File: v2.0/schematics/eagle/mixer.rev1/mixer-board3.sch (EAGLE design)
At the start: 5 parts, among them J1 RTN-1, J2 RTN-2, J3 SEND1, J4 SEND2

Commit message: Added stereo returns
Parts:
- added C1, C10, C11, C2, C4, C5, C7, C8: 100uF, _common:CE-USE5-8.5
- added C12, C3, C6, C9: (no value), _common:CC-US025-024X044
- added IC1, IC2: TL082P, _common:TL082P
- added JP1: (no value), pinhead:PINHD-2X8
- added R1, R13, R15, R7: 2.2K, _common:R
- added R10, R11, R12, R3, R4, R5, R6, R9: 10K, _common:R
- added R14, R16, R2, R8: 510, _common:R
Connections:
- new net +12V: JP1.5
- new net -12V: JP1.1
- new net 0V: J1.P$1, J1.P$2, J1.P$4, J2.P$1, J2.P$2, J2.P$4, JP1.3, R11.1, R12.1, R14.1, R16.1, R2.1, R5.1, R6.1, R8.1, RV1.1
- new net M2-LVL-2: JP1.9, RV1.2
- new net M2-LVL-3: JP1.7, RV1.3
- new net N$1: C1.+, J1.P$3, J1.P$6
- new net N$10: C2.-, R4.1
- new net N$11: IC2B.+IN, R10.2, R12.2
- new net N$12: IC2A.+IN, R11.2, R9.2
- new net N$13: C9.2, IC2A.-IN, R13.1, R14.2
- new net N$14: C10.+, C9.1, IC2A.OUT, R13.2
- new net N$15: C7.-, R9.1
- new net N$16: C8.-, R10.1
- new net N$17: C12.2, IC2B.-IN, R15.1, R16.2
- new net N$18: C11.+, C12.1, IC2B.OUT, R15.2
- new net N$19: C7.+, J2.P$3, J2.P$6
- new net N$2: C2.+, J1.P$5
- new net N$20: C8.+, J2.P$5
- new net N$3: C6.2, IC1B.-IN, R1.1, R2.2
- new net N$4: C5.+, C6.1, IC1B.OUT, R1.2
- new net N$5: IC1B.+IN, R4.2, R6.2
- new net N$6: IC1A.+IN, R3.2, R5.2
- new net N$7: C3.2, IC1A.-IN, R7.1, R8.2
- new net N$8: C1.-, R3.1
- new net N$9: C3.1, C4.+, IC1A.OUT, R7.2
- new net RTN1-L: C5.-, JP1.2
- new net RTN1-R: C4.-, JP1.4
- new net RTN2-L: C11.-, JP1.6
- new net RTN2-R: C10.-, JP1.8
- new net SEND1: JP1.11
- new net SEND2: JP1.13
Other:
- note added: "For mono in, push to first click"
- note added: "N/C"
- moved on the sheet: J1, J2, J3, J4, RV1

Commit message: Completed initial mixer schematic draft
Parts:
- added C13, C14, C15, C16: 22pF, _common:CC-US025-024X044
- added C17, C18: 100uF, _common:CE-USE2-5
- added C19, C20, C21, C22, C25, C26, C27, C28, C29, C30: 0.1uF, _common.v1:CC-US025-024X044
- added C23, C24: 10uF, _common.v1:CE-USE2-5
- added IC3, IC4: TL082P, _common:TL082P
- added R17, R18, R19, R20: 100K, _common:R
- added R21, R22: 22K, _common:R
- added R23, R24, R25, R26, R27, R28: 10K, _common:R
- C12, C3, C9: value (none) -> 100uF; device _common:CC-US025-024X044 -> _common:CE-USE5-8.5
- C5, C7, C8: value 100uF -> 22pF; device _common:CE-USE5-8.5 -> _common:CC-US025-024X044
- C6: value (none) -> 22pF
- R1, R7: value 2.2K -> 10K
- R10, R11, R12, R9: value 10K -> 10k
- R13, R15: value 2.2K -> 30k
- R14, R16: value 510 -> 30k
- R2, R8: value 510 -> 10K
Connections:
- new net N$21: C13.2, IC3A.-IN, R17.2, R19.2, R21.1
- new net N$22: C13.1, IC3A.OUT, R21.2, R23.1
- new net N$23: C15.2, IC3B.-IN, R23.2, R25.1
- new net N$24: C15.1, C17.-, IC3B.OUT, R25.2
- new net N$25: C14.2, IC4A.-IN, R18.2, R20.2, R22.1
- new net N$26: C14.1, IC4A.OUT, R22.2, R24.1
- new net N$27: C16.2, IC4B.-IN, R24.2, R26.1
- new net N$28: C16.1, C18.-, IC4B.OUT, R26.2
- new net OUT-LVL-1: C18.+, J4.P$3, R28.2
- new net OUT-LVL-6: C17.+, J3.P$3, R27.2
- net +12V: now also C19.1, C21.1, C23.+, C25.1, C27.1, C29.1
- net -12V: now also C20.2, C22.2, C24.-, C26.2, C28.2, C30.2
- net 0V: now also C19.2, C20.1, C21.2, C22.1, C23.-, C24.+, C25.2, C26.1, C27.2, C28.1, C29.2, C30.1, IC3A.+IN, IC3B.+IN, IC4A.+IN, IC4B.+IN, J3.P$1, J3.P$2, J4.P$1, J4.P$2, R10.1, R19.1, R20.1, R27.1, R28.1, R7.1, R9.1; no longer R14.1, R16.1, R2.1
- net N$10: now also R2.1; no longer R4.1
- net N$11: now also R4.2, R8.2; no longer R10.2, R12.2
- net N$12: now also R3.2, R7.2; no longer R11.2, R9.2
- net N$13: now also C7.2, R11.2, R15.1; no longer C9.2, R13.1, R14.2
- net N$14: now also C11.+, C7.1, R15.2; no longer C10.+, C9.1, R13.2
- net N$15: now also C3.-, R3.1; no longer C7.-, R9.1
- net N$16: now also C4.-, R4.1; no longer C8.-, R10.1
- net N$17: now also C8.2, R12.2, R16.1; no longer C12.2, R15.1, R16.2
- net N$18: now also C12.+, C8.1, R16.2; no longer C11.+, C12.1, R15.2
- net N$19: now also C3.+; no longer C7.+
- net N$20: now also C4.+; no longer C8.+
- net N$3: now also R10.2, R14.1; no longer R1.1, R2.2
- net N$4: now also C10.+, R14.2; no longer C5.+, R1.2
- net N$5: now also R2.2; no longer R4.2
- net N$6: now also R1.2; no longer R3.2
- net N$7: now also C5.2, R13.1, R9.2; no longer C3.2, R7.1, R8.2
- net N$8: now also R1.1; no longer R3.1
- net N$9: now also C5.1, C9.+, R13.2; no longer C3.1, C4.+, R7.2
- net RTN1-L: now also C10.-; no longer C5.-
- net RTN1-R: now also C9.-; no longer C4.-
- net RTN2-L: now also C12.-; no longer C11.-
- net RTN2-R: now also C11.-; no longer C10.-
- net SEND1: now also R17.1
- net SEND2: now also R18.1
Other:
- moved on the sheet: C1, C10, C11, C12, C2, C3, C4, C5, C6, C7, C8, C9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

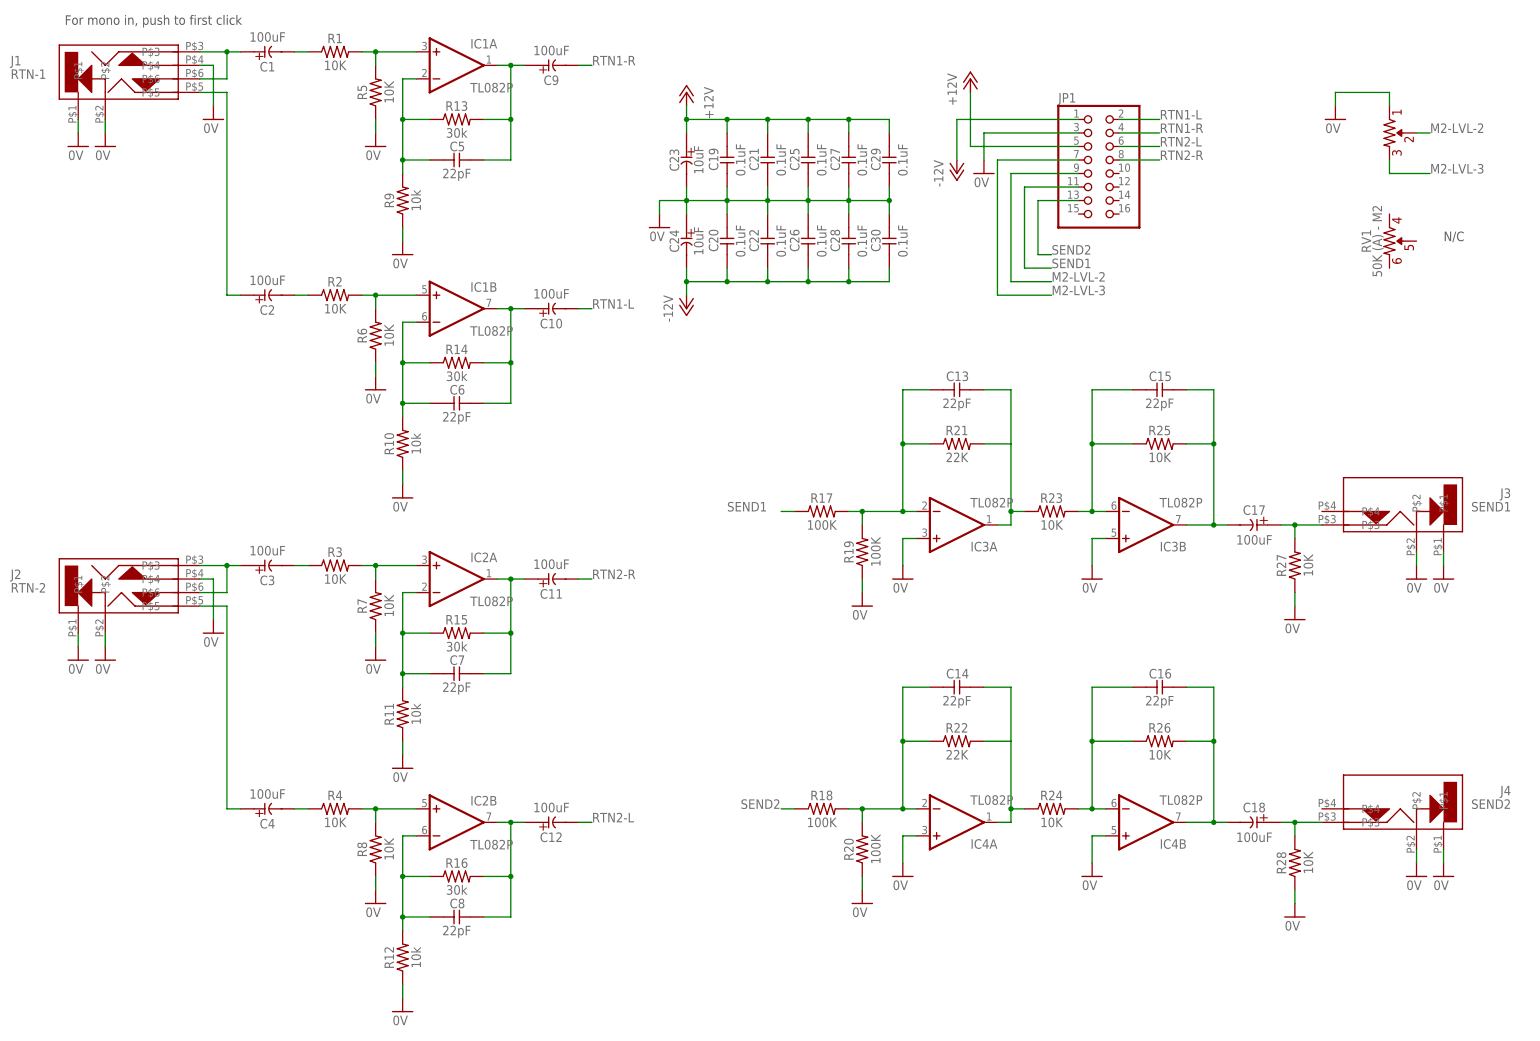
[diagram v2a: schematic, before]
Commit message: Updated VAR-ST; Added FX Crossfades; Ran error checks
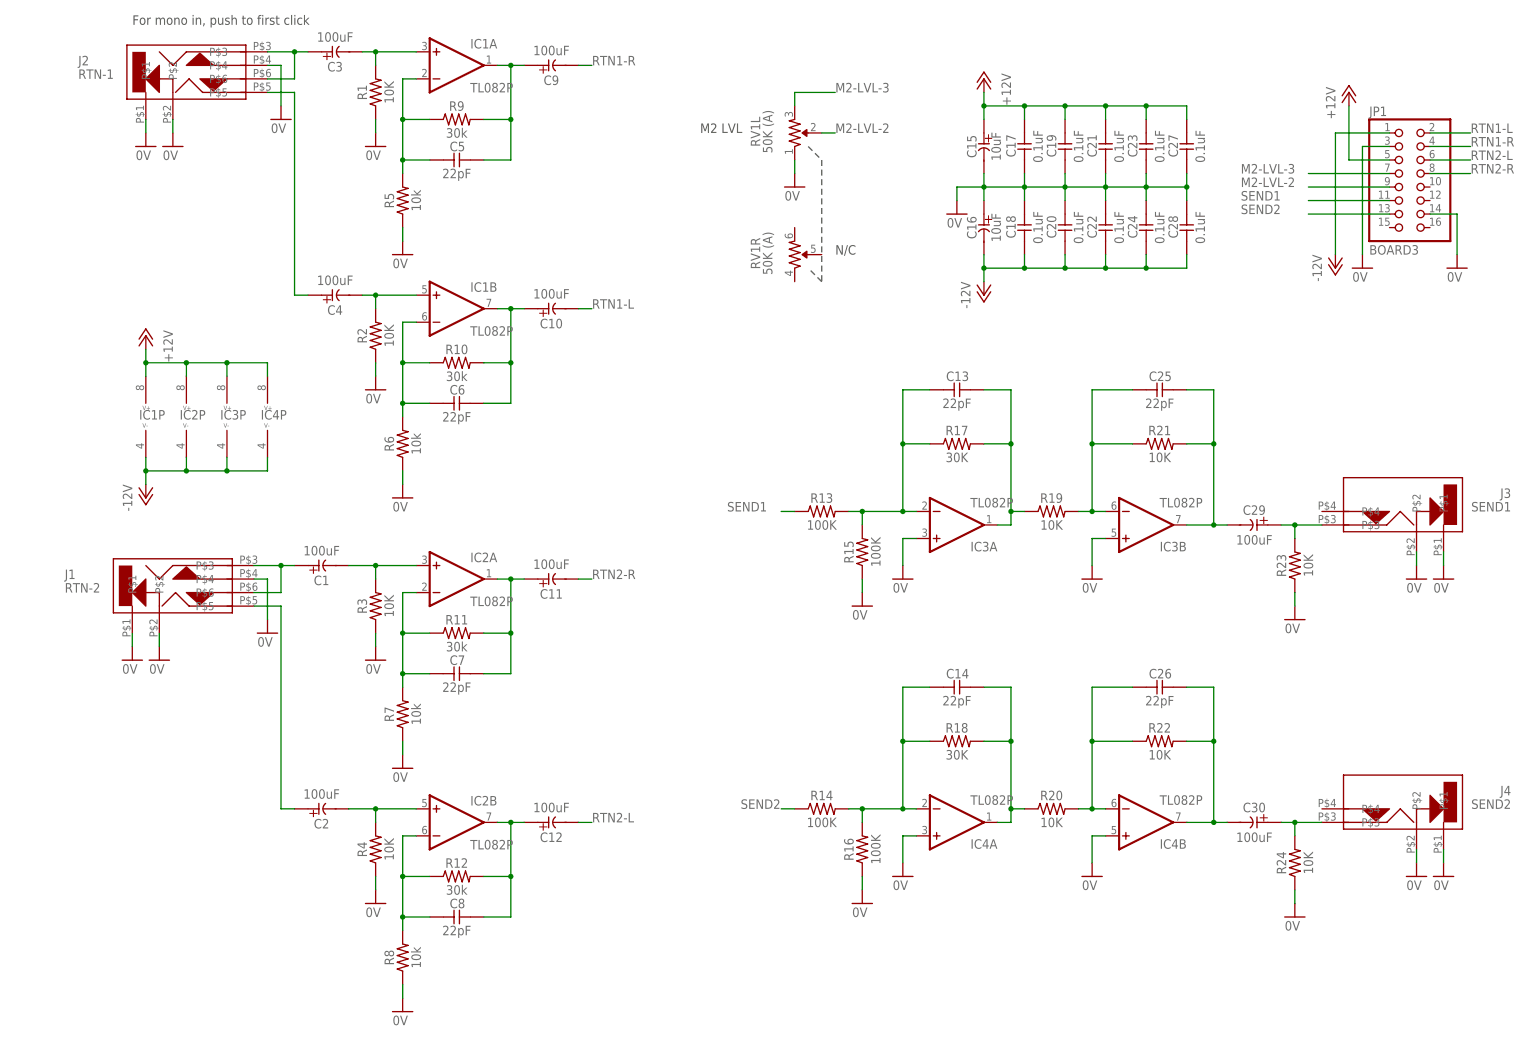
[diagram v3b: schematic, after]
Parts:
- removed R25, R26, R27, R28: 10K, _common:R
- C15, C16: value 22pF -> 10uF; device _common:CC-US025-024X044 -> _common.v1:CE-USE2-5
- C17, C18: value 100uF -> 0.1uF; device _common:CE-USE2-5 -> _common.v1:CC-US025-024X044
- C23, C24: value 10uF -> 0.1uF; device _common.v1:CE-USE2-5 -> _common.v1:CC-US025-024X044
- C25, C26: value 0.1uF -> 22pF; device _common.v1:CC-US025-024X044 -> _common:CC-US025-024X044
- C29, C30: value 0.1uF -> 100uF; device _common.v1:CC-US025-024X044 -> _common:CE-USE2-5
- J1: value RTN-1 -> RTN-2
- J2: value RTN-2 -> RTN-1
- JP1: value (none) -> BOARD3
- R10, R11, R12, R9: value 10k -> 30k
- R13, R14, R15, R16: value 30k -> 100K
- R17, R18: value 100K -> 30K
- R19, R20: value 100K -> 10K
- R21, R22: value 22K -> 10K
- R5, R6, R7, R8: value 10K -> 10k
- RV1: value 50K (A) - M2 -> 50K (A)
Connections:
- removed net N$11: IC2B.+IN, R4.2, R8.2
- removed net N$12: IC2A.+IN, R3.2, R7.2
- removed net N$5: IC1B.+IN, R2.2, R6.2
- removed net N$8: C1.-, R1.1
- net +12V: now also C15.+, C17.1, C23.1, IC1P.V+, IC2P.V+, IC3P.V+, IC4P.V+; no longer C23.+, C25.1, C29.1
- net -12V: now also C16.-, C18.2, C24.2, IC1P.V-, IC2P.V-, IC3P.V-, IC4P.V-; no longer C24.-, C26.2, C30.2
- net 0V: now also C15.-, C16.+, C17.2, C18.1, C23.2, C24.1, JP1.14, R1.1, R15.1, R16.1, R2.1, R23.1, R24.1, R3.1, R4.1, RV1L.1; no longer C23.-, C24.+, C25.2, C26.1, C29.2, C30.1, R10.1, R11.1, R12.1, R19.1, R20.1, R27.1, R28.1, R9.1, RV1.1
- net M2-LVL-2: now also RV1L.2; no longer RV1.2
- net M2-LVL-3: now also RV1L.3; no longer RV1.3
- net N$10: now also C4.-, IC1B.+IN, R2.2; no longer C2.-, R2.1
- net N$13: now also R11.1, R7.2; no longer R11.2, R15.1
- net N$14: now also R11.2; no longer R15.2
- net N$15: now also C1.-, IC2A.+IN, R3.2; no longer C3.-, R3.1
- net N$16: now also C2.-, IC2B.+IN, R4.2; no longer C4.-, R4.1
- net N$17: now also R12.1, R8.2; no longer R12.2, R16.1
- net N$18: now also R12.2; no longer R16.2
- net N$21: now also R13.2, R15.2, R17.1; no longer R17.2, R19.2, R21.1
- net N$22: now also R17.2, R19.1; no longer R21.2, R23.1
- net N$23: now also C25.2, R19.2, R21.1; no longer C15.2, R23.2, R25.1
- net N$24: now also C25.1, C29.-, R21.2; no longer C15.1, C17.-, R25.2
- net N$25: now also R14.2, R16.2, R18.1; no longer R18.2, R20.2, R22.1
- net N$26: now also R18.2, R20.1; no longer R22.2, R24.1
- net N$27: now also C26.2, R20.2, R22.1; no longer C16.2, R24.2, R26.1
- net N$28: now also C26.1, C30.-, R22.2; no longer C16.1, C18.-, R26.2
- net N$3: now also R10.1, R6.2; no longer R10.2, R14.1
- net N$4: now also R10.2; no longer R14.2
- net N$6: now also C3.-; no longer R5.2
- net N$7: now also R5.2, R9.1; no longer R13.1, R9.2
- net N$9: now also R9.2; no longer R13.2
- net OUT-LVL-1: now also C30.+, R24.2; no longer C18.+, R28.2
- net OUT-LVL-6: now also C29.+, R23.2; no longer C17.+, R27.2
- net SEND1: now also R13.1; no longer R17.1
- net SEND2: now also R14.1; no longer R18.1
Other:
- note added: "M2 LVL"
- moved on the sheet: C1, C15, C16, C17, C18, C19, C2, C20, C21, C22, C23, C24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

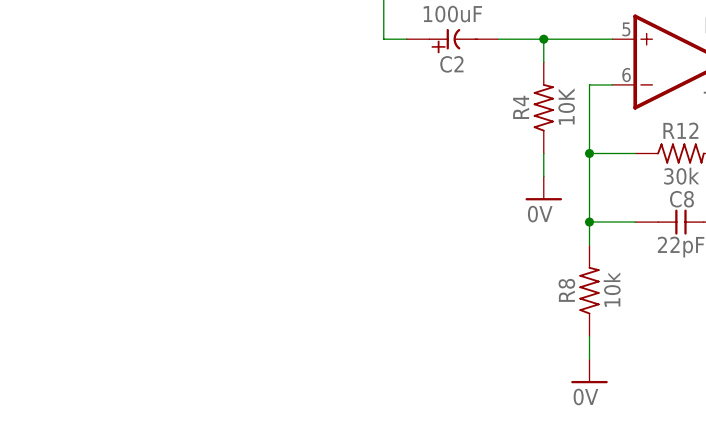
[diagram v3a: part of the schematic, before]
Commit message: Added schem titles
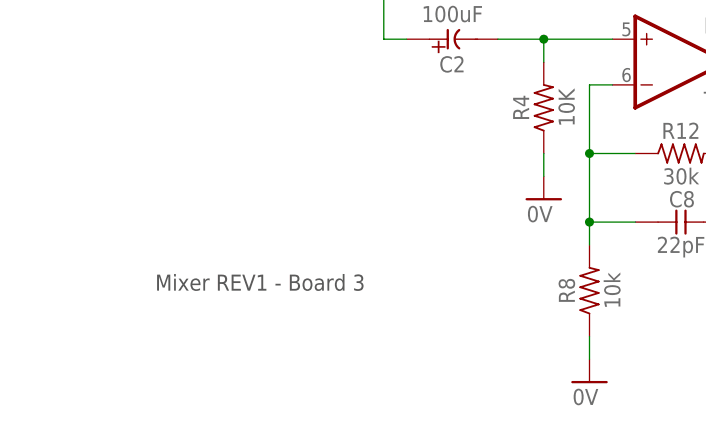
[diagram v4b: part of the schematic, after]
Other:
- note added: "Mixer REV1 - Board 3"
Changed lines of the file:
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@@
 <wire x1="177.8" y1="129.54" x2="177.8" y2="106.68" width="0.1524" layer="97" style="shortdash"/>
 <wire x1="177.8" y1="106.68" x2="175.26" y2="109.22" width="0.1524" layer="97" style="shortdash"/>
+<text x="50.8" y="-20.32" size="1.778" layer="97">Mixer REV1 - Board 3</text>
 </plain>
 <instances>

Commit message: Updated cap packages
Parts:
- C29, C30: device _common:CE-USE2-5 -> _common:CE-USE5-8.5
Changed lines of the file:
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@@
 <part name="GND19" library="supply1" library_urn="urn:adsk.eagle:library:371" deviceset="0V" device=""/>
 <part name="GND20" library="supply1" library_urn="urn:adsk.eagle:library:371" deviceset="0V" device=""/>
-<part name="C29" library="_common" deviceset="CE-US" device="E2-5" value="100uF"/>
+<part name="C29" library="_common" deviceset="CE-US" device="E5-8.5" value="100uF"/>
 <part name="R23" library="_common" deviceset="R" device="" value="10K"/>
 <part name="GND21" library="supply1" library_urn="urn:adsk.eagle:library:371" deviceset="0V" device=""/>
@@
 <part name="GND23" library="supply1" library_urn="urn:adsk.eagle:library:371" deviceset="0V" device=""/>
 <part name="GND24" library="supply1" library_urn="urn:adsk.eagle:library:371" deviceset="0V" device=""/>
-<part name="C30" library="_common" deviceset="CE-US" device="E2-5" value="100uF"/>
+<part name="C30" library="_common" deviceset="CE-US" device="E5-8.5" value="100uF"/>
 <part name="R24" library="_common" deviceset="R" device="" value="10K"/>
 <part name="GND25" library="supply1" library_urn="urn:adsk.eagle:library:371" deviceset="0V" device=""/>
